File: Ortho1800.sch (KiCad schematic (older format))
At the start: 214 parts

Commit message: Adding led matrix
Add led matrix and BT connector will see to add HC05 module later...
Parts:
- added D? (x90): LED, symbol Device:LED
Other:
- note added: "Battery management"
- moved on the sheet: C?, J?, R?, SW?A, U?, Y?

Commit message: Symbole switch
Symbole switch changed with switch with led to simplify schematic.
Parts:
- removed D? (x90): LED, symbol Device:LED
- removed SW? (x98): SW_SPST, symbol Ortho1800-rescue:SW_SPST-Switch
- added R? (x4): R_Small, symbol Device:R_Small
- added SW? (x98): SW_WITHLED, symbol sw_withled:SW_WITHLED
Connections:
- wire segments 706 -> 708
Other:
- moved on the sheet: C?, J?, R?, SW?A, U?, Y?

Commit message: .
Work from home try led schematic
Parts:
- SW? (x98): symbol sw_withled:SW_WITHLED -> Ortho1800-rescue:SW_WITHLED-sw_withled
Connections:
- wire segments 708 -> 758

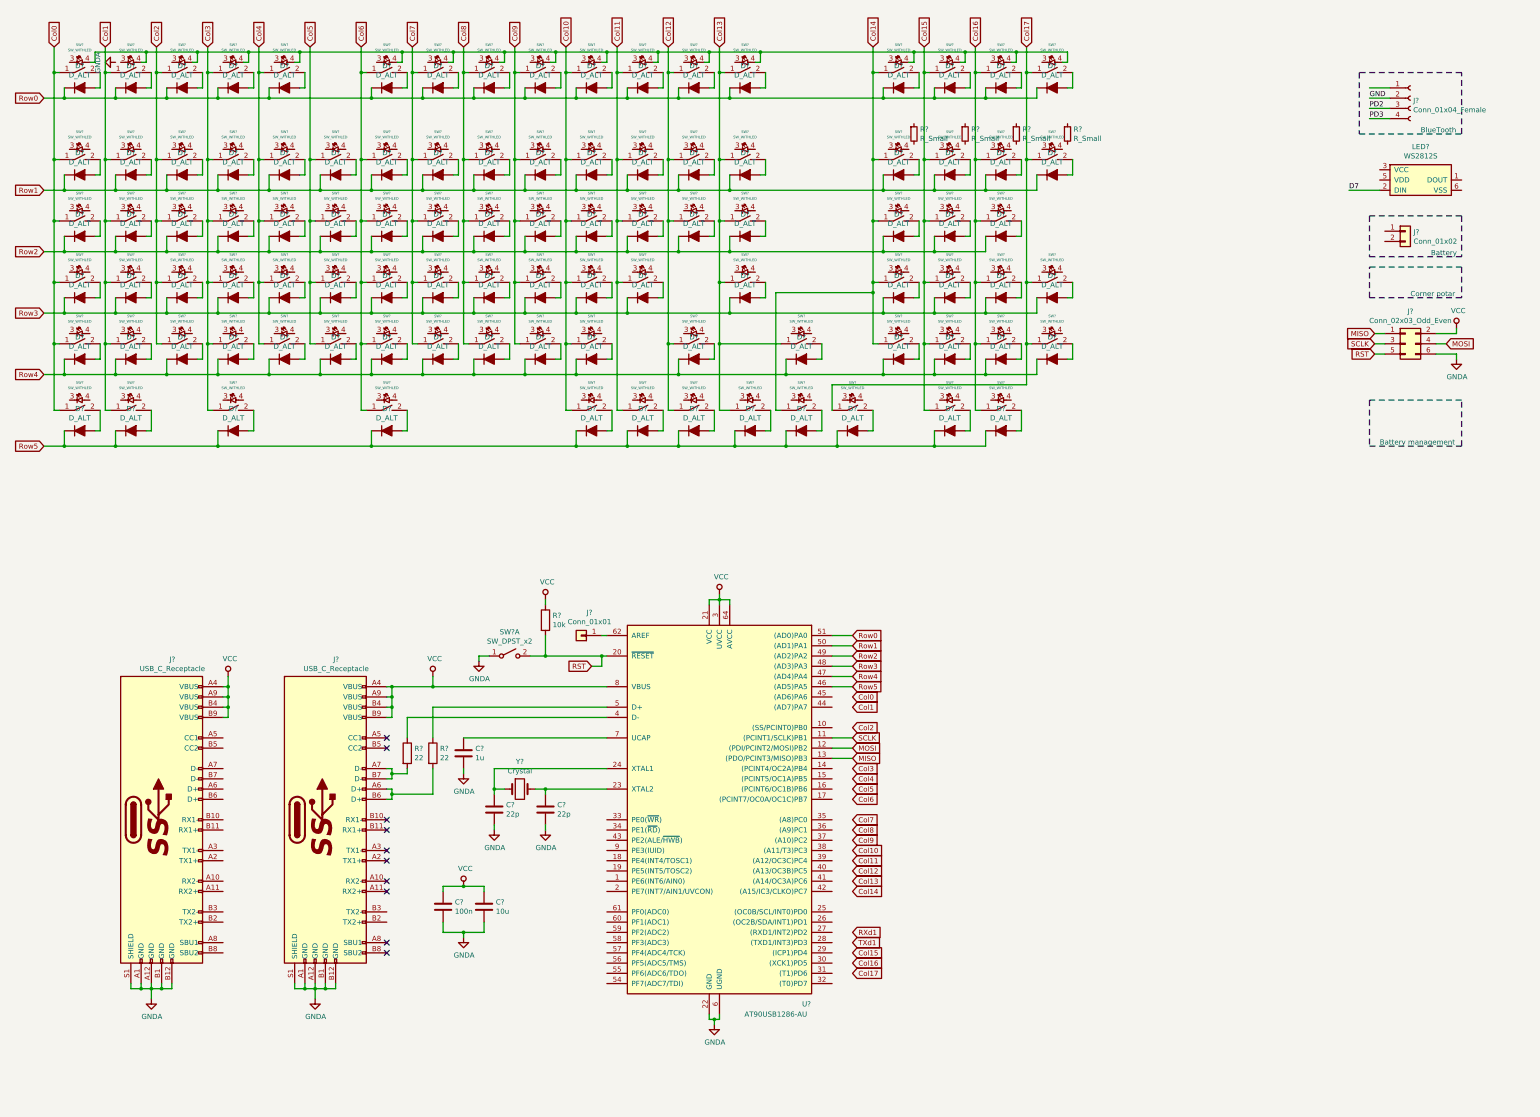
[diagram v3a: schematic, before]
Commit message: Remap update ongoing
Remap the existing keyboard schematic
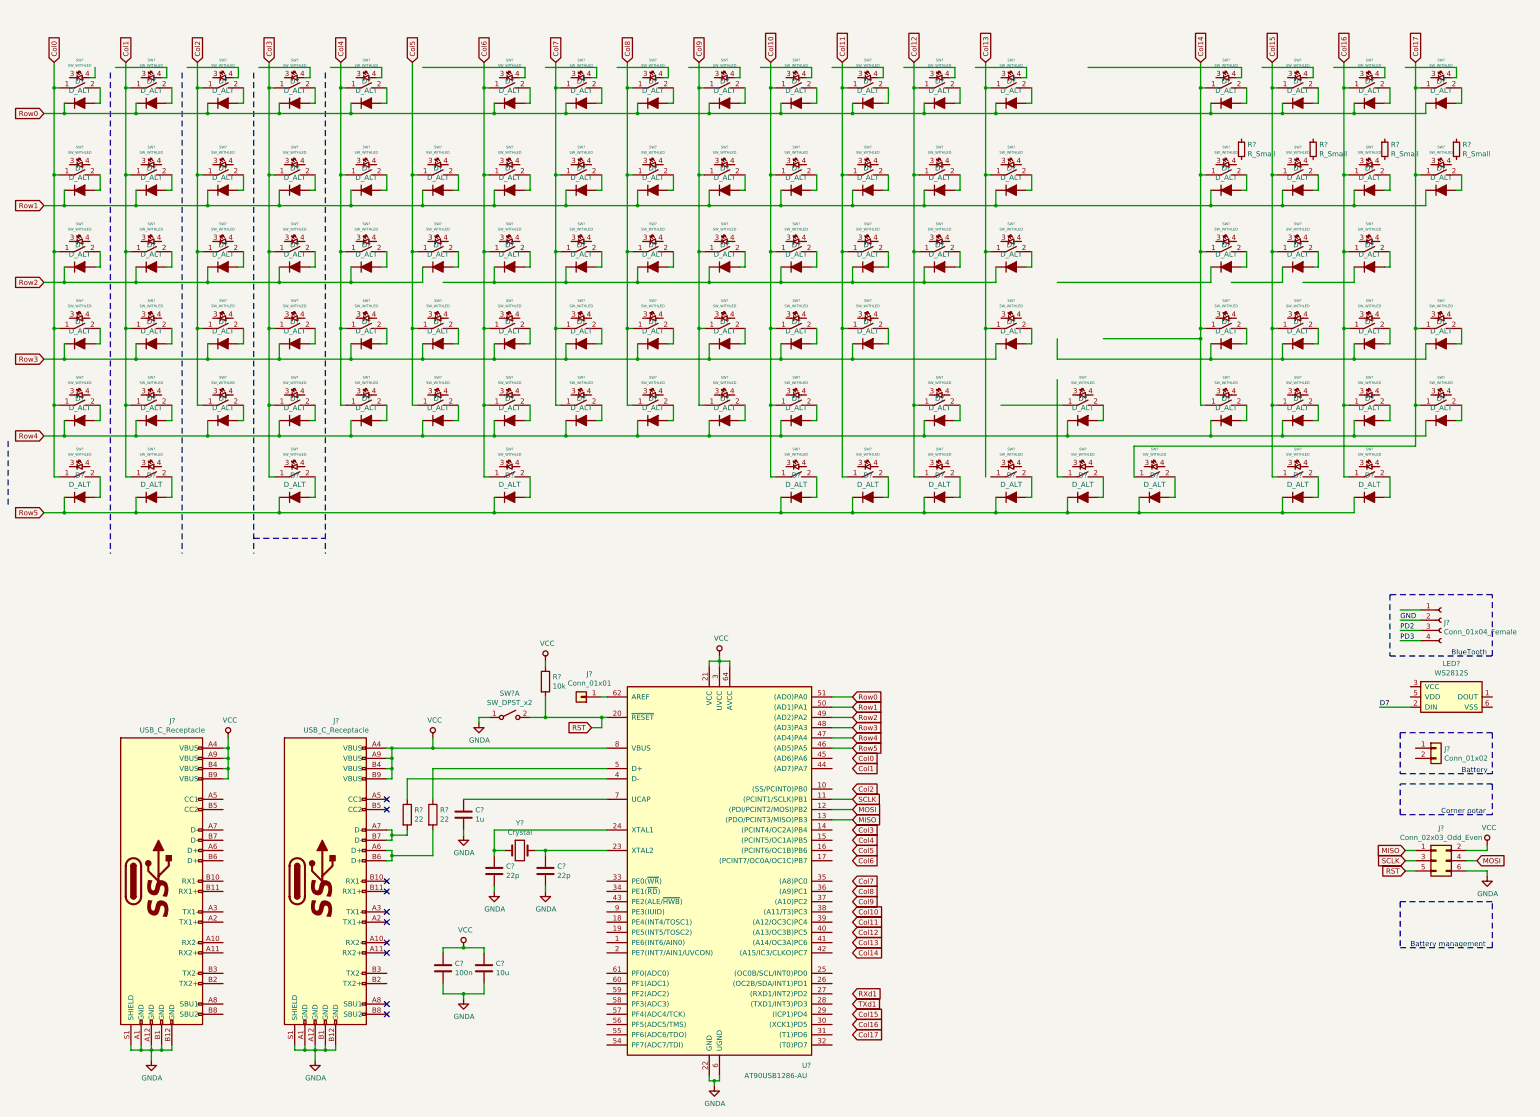
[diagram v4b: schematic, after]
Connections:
- wire segments 758 -> 757
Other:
- moved on the sheet: C?, D?, J?, LED?, R?, SW?, SW?A, U?, Y?

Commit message: Schematic Update
Need Footprints for switch
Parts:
- removed R? (x4): R_Small, symbol Device:R_Small
- added D101: LED_Small, symbol Device:LED_Small
- added D102, D103: LED_Small, LED_SMD:LED_1206_3216Metric_Pad1.42x1.75mm_HandSolder, symbol Device:LED_Small
- added D102_1, D103_2: LED_Small, LED_SMD:LED_1206_3216Metric_ReverseMount_Hole1.8x2.4mm, symbol Device:LED_Small
- added D87, D88: LED, symbol Device:LED
- added J3, J7, J8, PD2, PD3, PE3, PE4, PE5, PE6, PE7, PF0, PF1, PF2, PF3, PF4, PF5, PF6: (no value), TestPoint:TestPoint_Pad_D1.5mm, symbol Ortho1800-rescue:Conn_01x01-Connector_Generic
- added Q1: IRF7403, Package_SO:SOIC-8_3.9x4.9mm_P1.27mm, symbol Transistor_FET:IRF7403
- added R1, R2, R3, R4, R5, R6: R, Resistor_SMD:R_0805_2012Metric_Pad1.15x1.40mm_HandSolder, symbol Device:R
- added R12: 2k, Resistor_SMD:R_0805_2012Metric_Pad1.15x1.40mm_HandSolder, symbol Device:R
- added R13: 10k, Resistor_SMD:R_0805_2012Metric_Pad1.15x1.40mm_HandSolder, symbol Ortho1800-rescue:R-Device
- added R14: 330, Resistor_SMD:R_0805_2012Metric_Pad1.15x1.40mm_HandSolder, symbol Ortho1800-rescue:R-Device
- added R15: 22, Resistor_SMD:R_0805_2012Metric_Pad1.15x1.40mm_HandSolder, symbol Ortho1800-rescue:R-Device
- added R7: 10k, Resistor_SMD:R_0805_2012Metric_Pad1.15x1.40mm_HandSolder, symbol Device:R
- added R9: 330, Resistor_SMD:R_0805_2012Metric_Pad1.15x1.40mm_HandSolder, symbol Device:R
- added U1: LTC4054ES5-4.2, Package_TO_SOT_SMD:TSOT-23-5, symbol Battery_Management:LTC4054ES5-4.2
- C1, C2, C3, C4, C5: renamed from C?; footprint (none) -> Capacitor_SMD:C_0805_2012Metric
- D1, D10, D100, D11, D12, D13, D14, D15, D16, D17, D18, D19, D2, D20, D21, D22, D23, D24, D25, D26, D27, D28, D29, D3, D30, D31, D32, D33, D34, D35, D36, D37, D38, D39, D4, D40, D41, D42, D43, D44, D45, D46, D47, D48, D49, D5, D50, D51, D52, D53, D54, D55, D56, D57, D58, D59, D6, D60, D61, D62, D63, D64, D65, D66, D67, D68, D69, D7, D70, D71, D72, D73, D74, D75, D76, D77, D78, D79, D8, D80, D81, D82, D83, D84, D85, D86, D89, D9, D90, D91, D92, D93, D94, D95, D96, D97, D98, D99: renamed from D?; footprint (none) -> Diode_SMD:D_SOD-123F
- J1: renamed from J?; footprint (none) -> Connector_PinHeader_2.54mm:PinHeader_1x04_P2.54mm_Vertical
- J12: renamed from J?; footprint (none) -> Connector_PinSocket_2.54mm:PinSocket_2x03_P2.54mm_Vertical
- J2: renamed from J?; footprint (none) -> TestPoint:TestPoint_Pad_D1.5mm
- J4: renamed from J?; footprint (none) -> Connector_JST:JST_EH_B02B-EH-A_1x02_P2.50mm_Vertical
- R10, R11, R8: renamed from R?; footprint (none) -> Resistor_SMD:R_0805_2012Metric_Pad1.15x1.40mm_HandSolder
- SW99: renamed from SW?; footprint (none) -> Button_Switch_SMD:SW_SPST_TL3342
- USB1, USB2: renamed from J?; footprint (none) -> Connector_USB:USB_C_Receptacle_Amphenol_12401548E4-2A_CircularHoles
- Y1: renamed from Y?; footprint (none) -> Crystal:Crystal_SMD_HC49-SD
- gave numbers to parts that had none: 100
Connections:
- net labels added: Led1, Led2, Led3, Led4, Led5, Led6, WS2812, uLed
- net labels removed: D7, GND, PD2, PD3
- wire segments 757 -> 929
- no-connect marks 10 -> 29
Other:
- note added: "98 led sw + 2 leds = 100 leds\n"
- note removed: "Battery"
- moved on the sheet: C4, C5, J1, J12, J4, LED1
